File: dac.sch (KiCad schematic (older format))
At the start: 46 parts, among them U15 OPA4172, U4 OPA4172, U8 DAC8568C

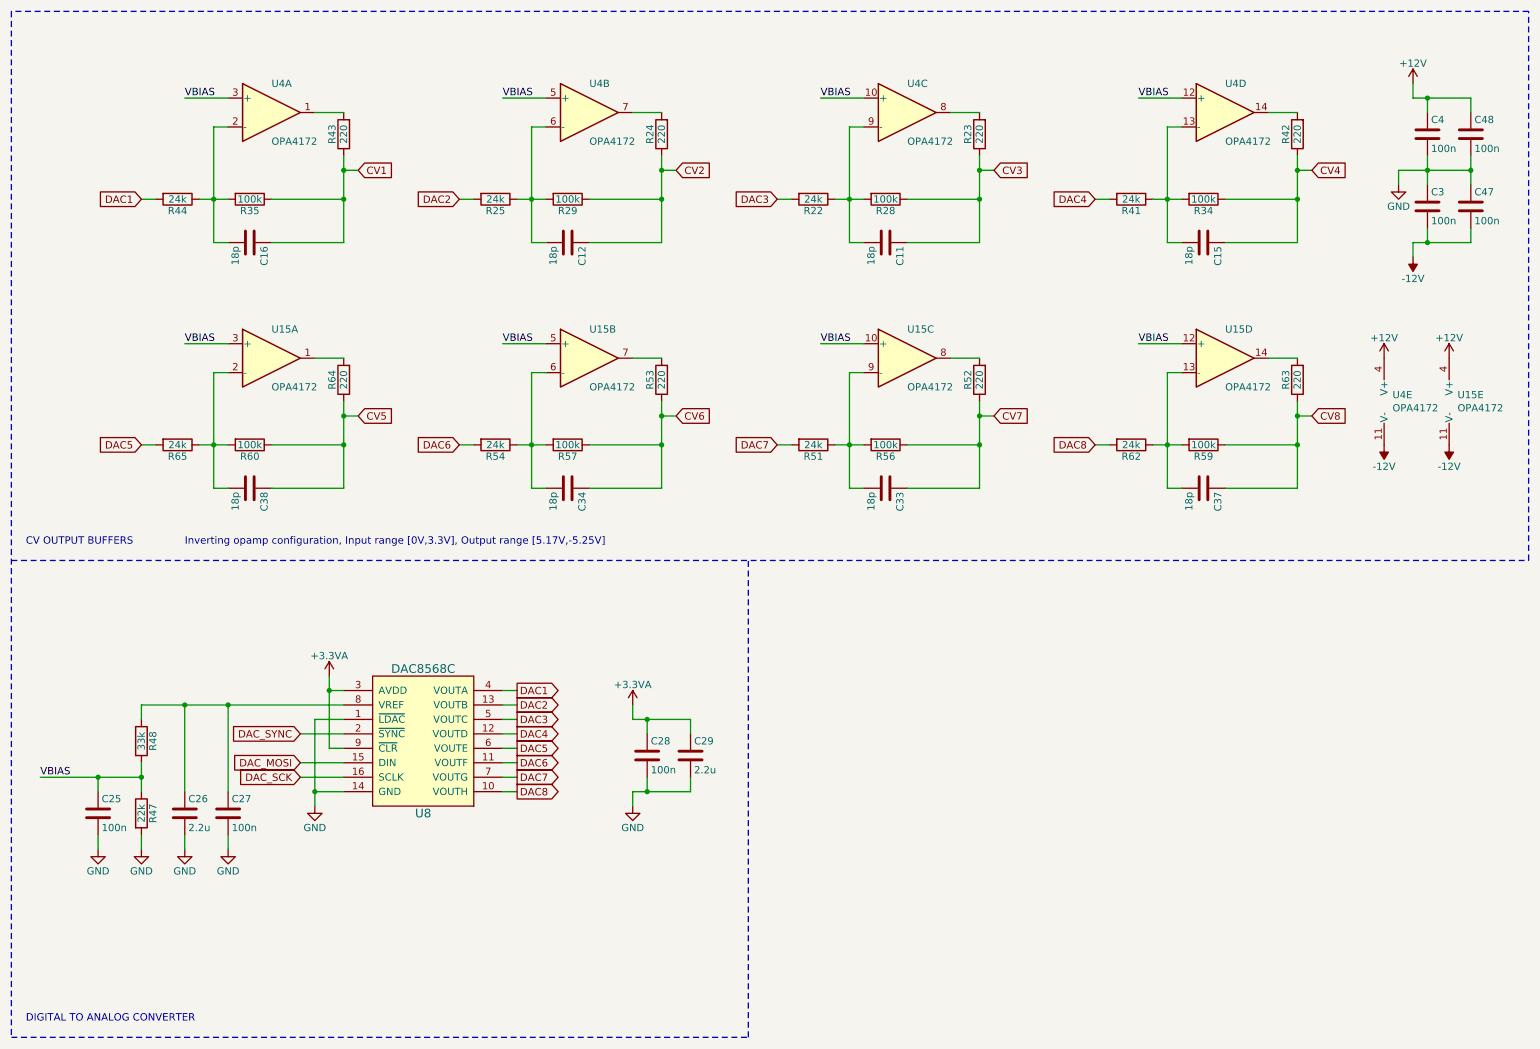
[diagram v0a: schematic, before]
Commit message: fixed feedback capacitors
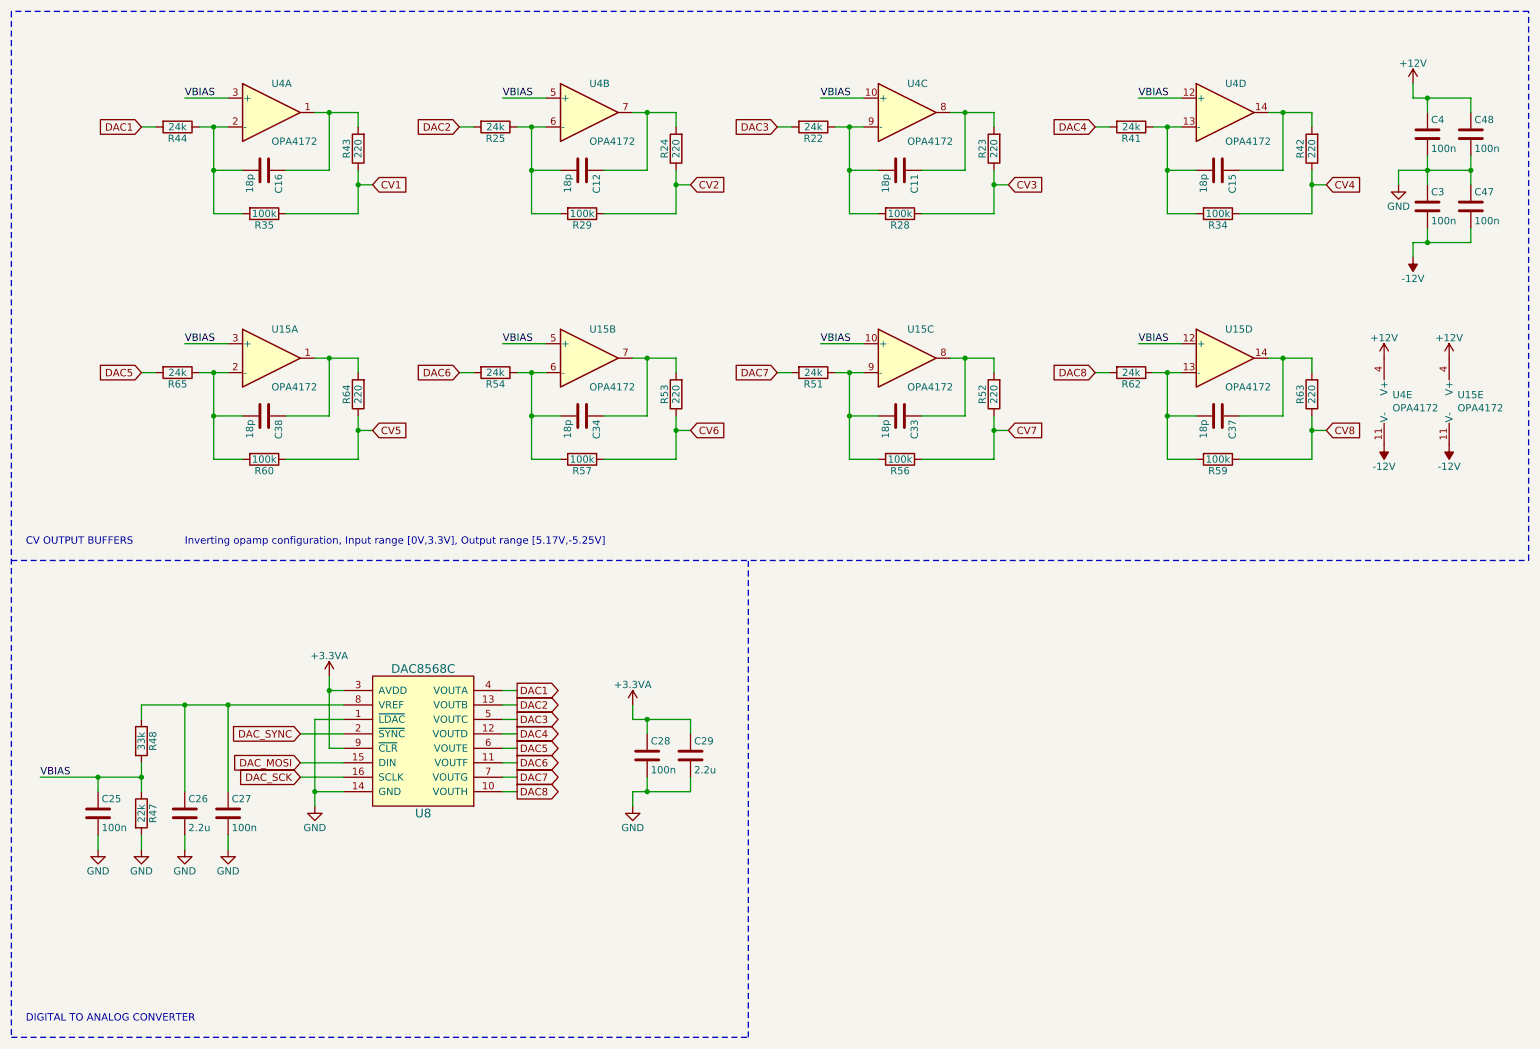
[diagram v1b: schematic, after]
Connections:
- net CV1: no longer C16.1
- net CV2: no longer C12.1
- net CV3: no longer C11.1
- net CV4: no longer C15.1
- net CV5: no longer C38.1
- net CV6: no longer C34.1
- net CV7: no longer C33.1
- net CV8: no longer C37.1
- net at R24.2, U4.7: now also C12.1
- net at R42.2, U4.14: now also C15.1
- net at R53.2, U15.7: now also C34.1
- net at R43.2, U4.1: now also C16.1
- net at R23.2, U4.8: now also C11.1
- net at R64.2, U15.1: now also C38.1
- net at R52.2, U15.8: now also C33.1
- net at R63.2, U15.14: now also C37.1
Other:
- moved on the sheet: C11, C12, C15, C16, C33, C34, C37, C38, R22, R23, R24, R25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

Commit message: updated component values and revision
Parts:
- U15, U4: MFN (none) -> Texas Instruments; MFP (none) -> OPA4172IDR; Package (none) -> SOIC-14

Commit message: small changes
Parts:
- C26, C29: footprint w_capacitor:C_0805 -> w_capacitor:C_0603
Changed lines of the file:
@@
 F 0 "C29" H 5325 5850 50  0000 L CNN
 F 1 "2.2u" H 5325 5650 50  0000 L CNN
-F 2 "w_capacitor:C_0805" H 5338 5600 50  0001 C CNN
+F 2 "w_capacitor:C_0603" H 5338 5600 50  0001 C CNN
 F 3 "http://datasheet.octopart.com/C2012X5R1A225K085AA-TDK-datasheet-41194876.pdf" H 5300 5750 50  0001 C CNN
 F 4 "TDK" H 5325 5950 50  0001 C CNN "MFN"
@@
 F 0 "C26" H 1825 6250 50  0000 L CNN
 F 1 "2.2u" H 1825 6050 50  0000 L CNN
-F 2 "w_capacitor:C_0805" H 1838 6000 50  0001 C CNN
+F 2 "w_capacitor:C_0603" H 1838 6000 50  0001 C CNN
 F 3 "http://datasheet.octopart.com/C2012X5R1A225K085AA-TDK-datasheet-41194876.pdf" H 1800 6150 50  0001 C CNN
 F 4 "TDK" H 1825 6350 50  0001 C CNN "MFN"
